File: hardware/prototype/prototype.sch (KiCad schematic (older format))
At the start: 68 parts, among them CON1 BARREL_JACK, P1 CONN_01X06, U1 MAX7221

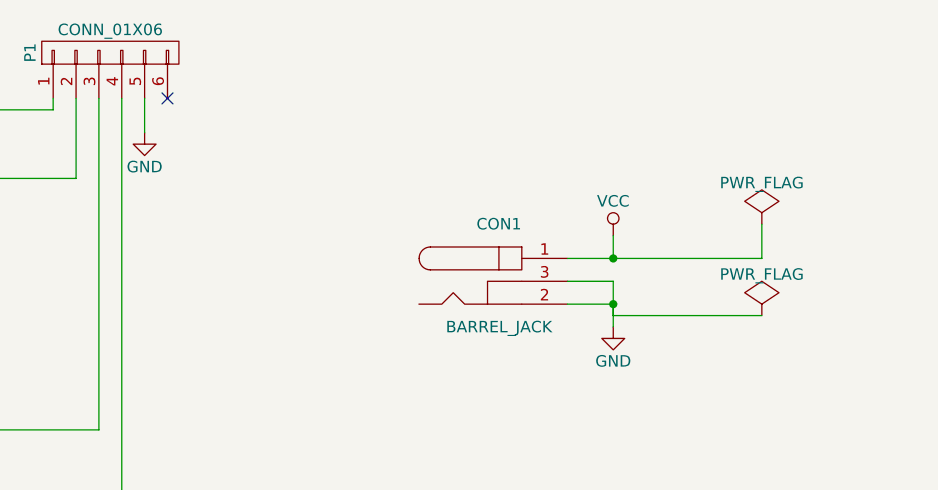
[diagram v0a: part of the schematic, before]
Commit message: Include the footprint modules, and assign footprints to all components.
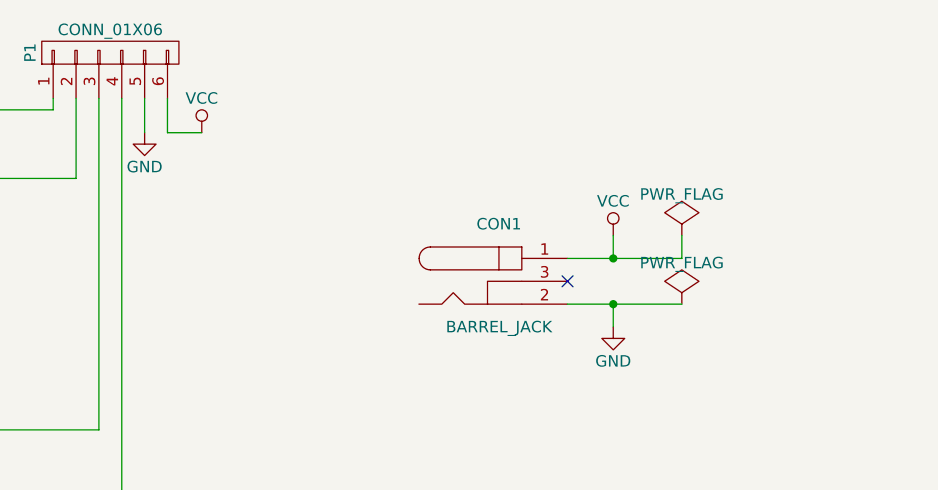
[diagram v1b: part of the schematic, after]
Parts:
- CON1: footprint (none) -> Connect:BARREL_JACK
- D1, D10, D11, D12, D13, D14, D15, D16, D17, D18, D19, D2, D20, D21, D22, D23, D24, D25, D26, D27, D28, D29, D3, D30, D31, D32, D33, D34, D35, D36, D37, D38, D39, D4, D40, D41, D42, D43, D44, D45, D46, D47, D48, D49, D5, D50, D51, D52, D53, D54, D55, D56, D57, D58, D59, D6, D60, D61, D62, D63, D64, D7, D8, D9: footprint (none) -> LEDs:LED-5MM
- P1: footprint (none) -> Pin_Headers:Pin_Header_Angled_1x06
- RSET1: footprint (none) -> Resistors_ThroughHole:Resistor_Horizontal_RM10mm
- U1: footprint MODULE -> DIL24:DIL24
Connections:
- net GND: no longer CON1.3
- net VCC: now also P1.6 (P6)
